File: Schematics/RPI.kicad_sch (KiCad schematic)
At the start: 1 part, among them J1 RPi GPIO

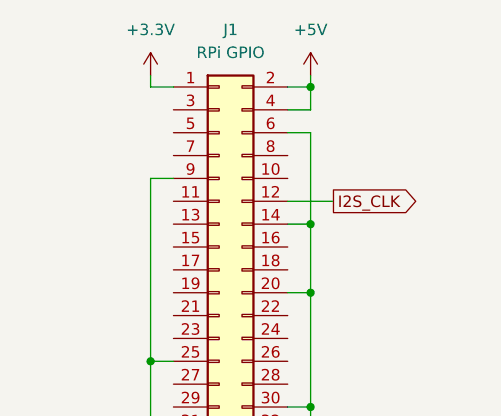
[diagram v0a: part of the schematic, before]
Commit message: Added recommended op-amps
Added recommended op-amps (without values) with dual mono TS in and out
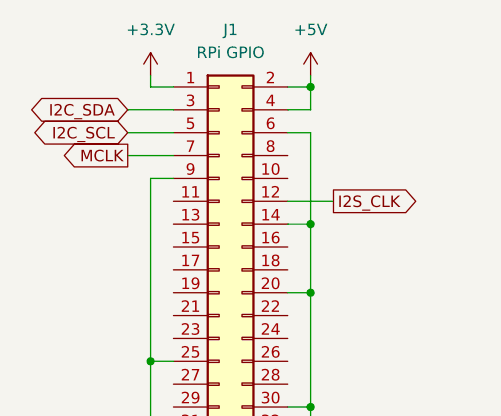
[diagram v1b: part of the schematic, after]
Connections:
- net I2C_SDA: now reaches J1.3 (Pin_3)
- net I2C_SCL: now reaches J1.5 (Pin_5)
- net MCLK: now reaches J1.7 (Pin_7)

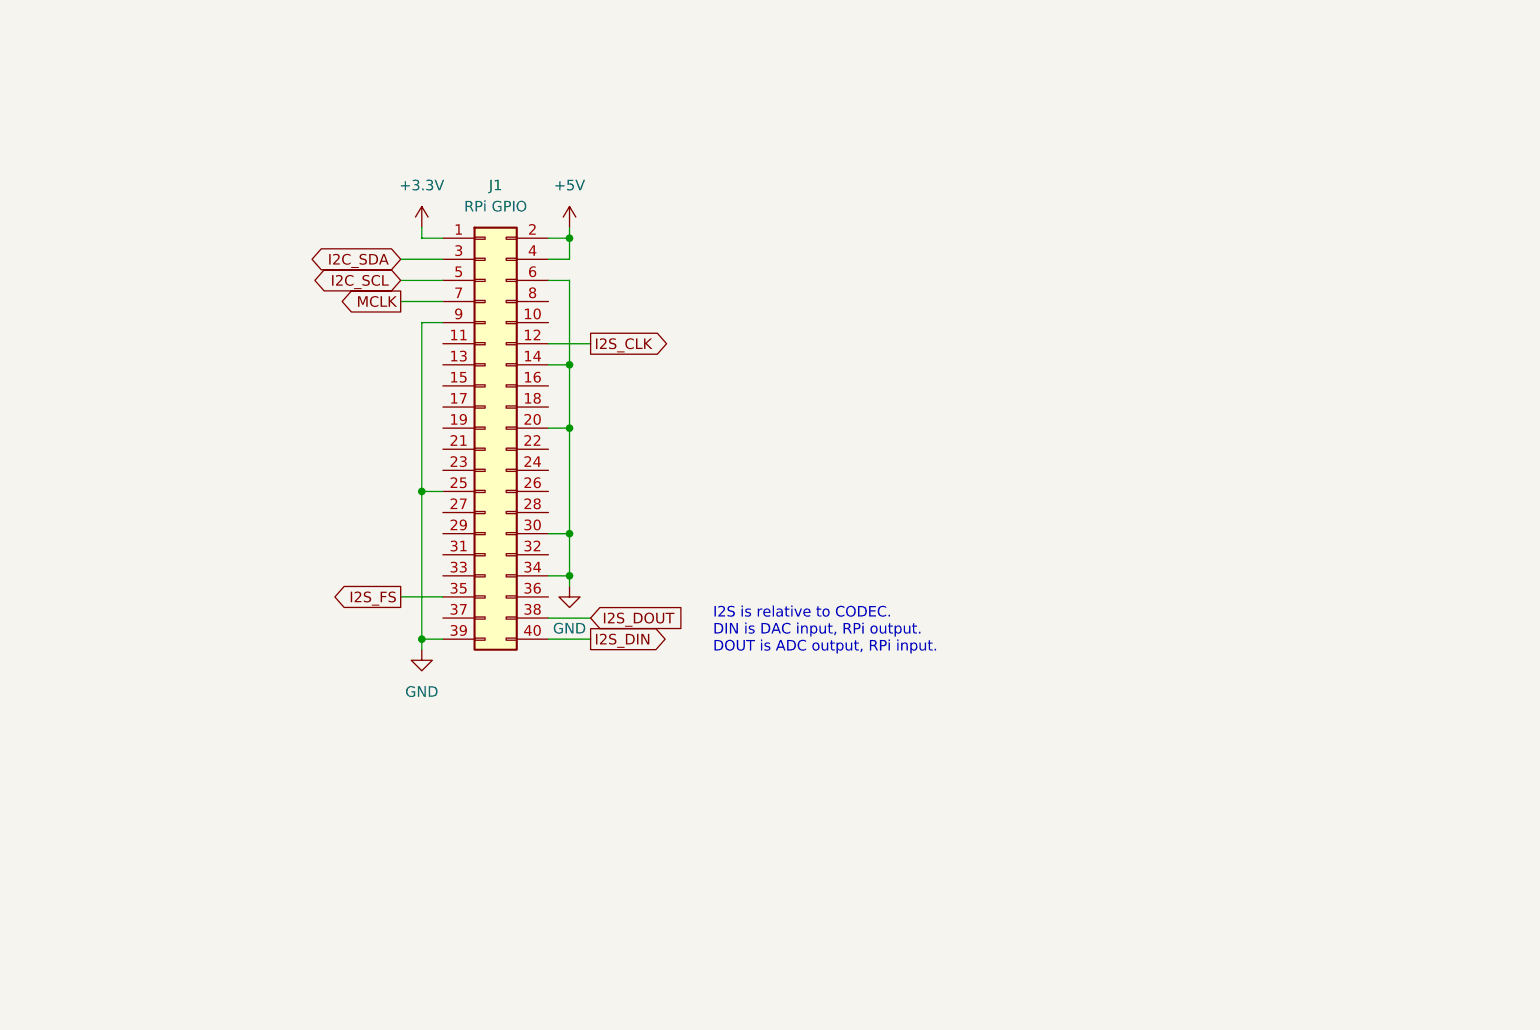
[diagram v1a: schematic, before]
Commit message: Input Buffer & EEPROM
line and instrument level buffers for the input added. EEPROM added and credits attributed !
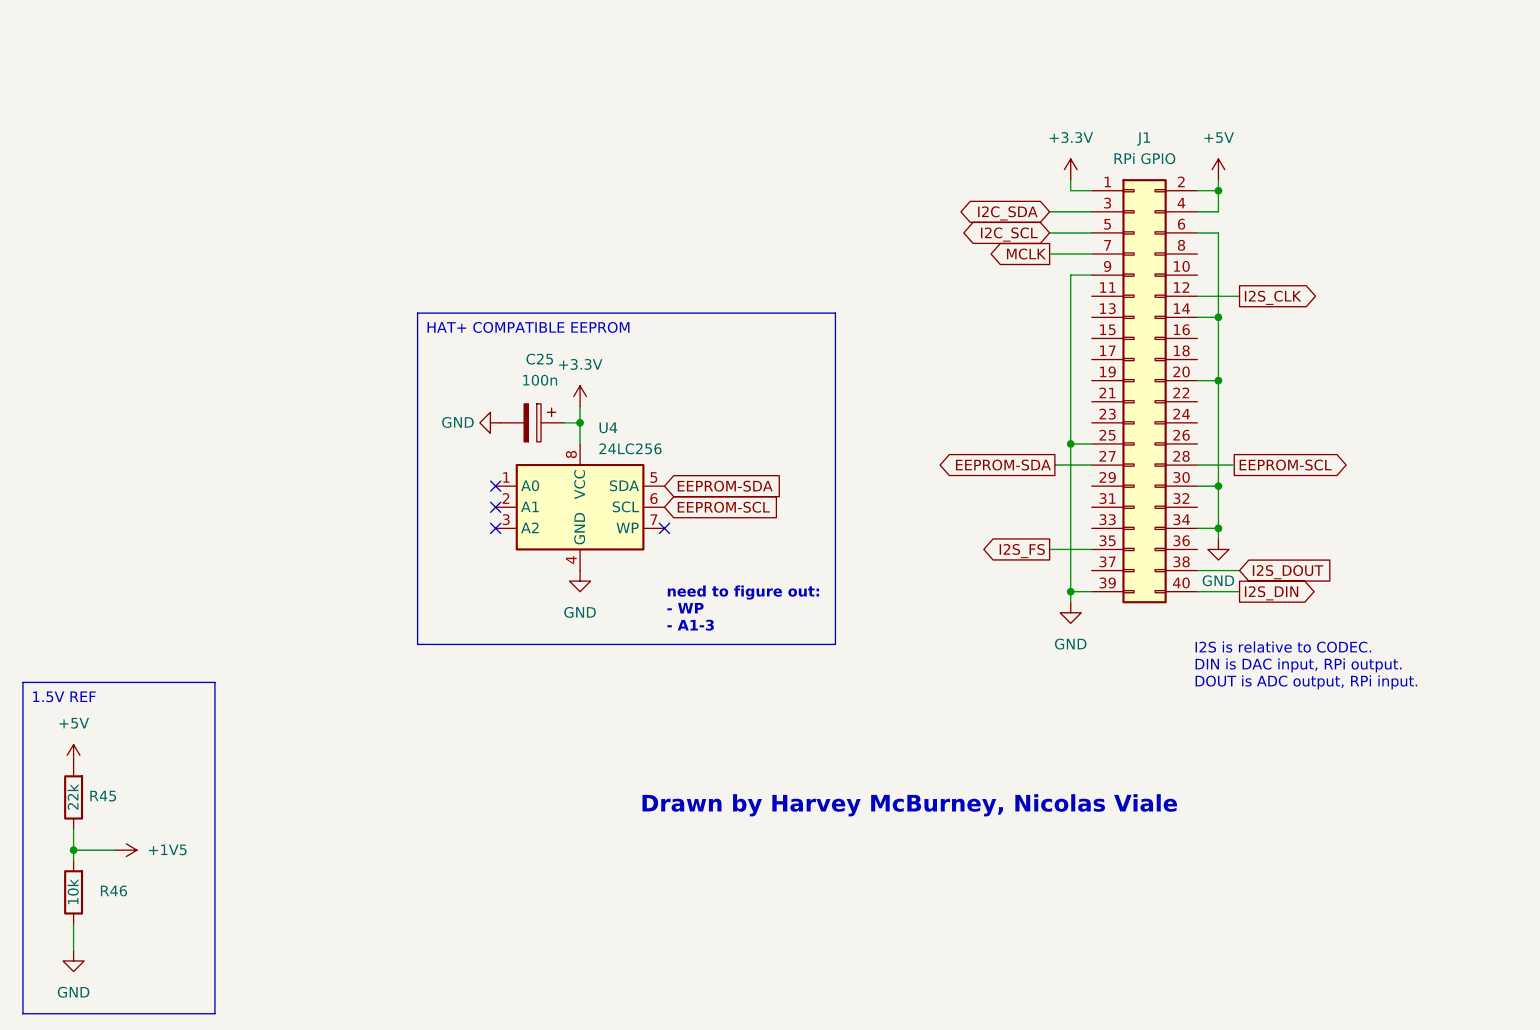
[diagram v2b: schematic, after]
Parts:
- added C25: 100n, symbol Device:C_Polarized
- added R45: 22k, symbol Device:R
- added R46: 10k, symbol Device:R
- added U4: 24LC256, symbol Memory_EEPROM:24LC256
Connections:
- net +3.3V: now also C25.1, U4.8 (VCC)
- net +5V: now also R45.2
- net GND: now also C25.2, R46.1, U4.4 (GND)
- net EEPROM-SDA: now reaches J1.27 (Pin_27)
- net EEPROM-SDA: now also U4.5 (SDA)
- net EEPROM-SCL: now reaches J1.28 (Pin_28)
- net EEPROM-SCL: now also U4.6 (SCL)
- new net +1V5: R45.1, R46.2
- no-connect marks 0 -> 4
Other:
- note added: "Drawn by Harvey McBurney, Nicolas Viale"
- note added: "need to figure out: - WP - A1-3"
- title: (none) -> Raspberry Pi GPIO pinout
- moved on the sheet: J1

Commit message: Schematic Update
Added EEPROM connections
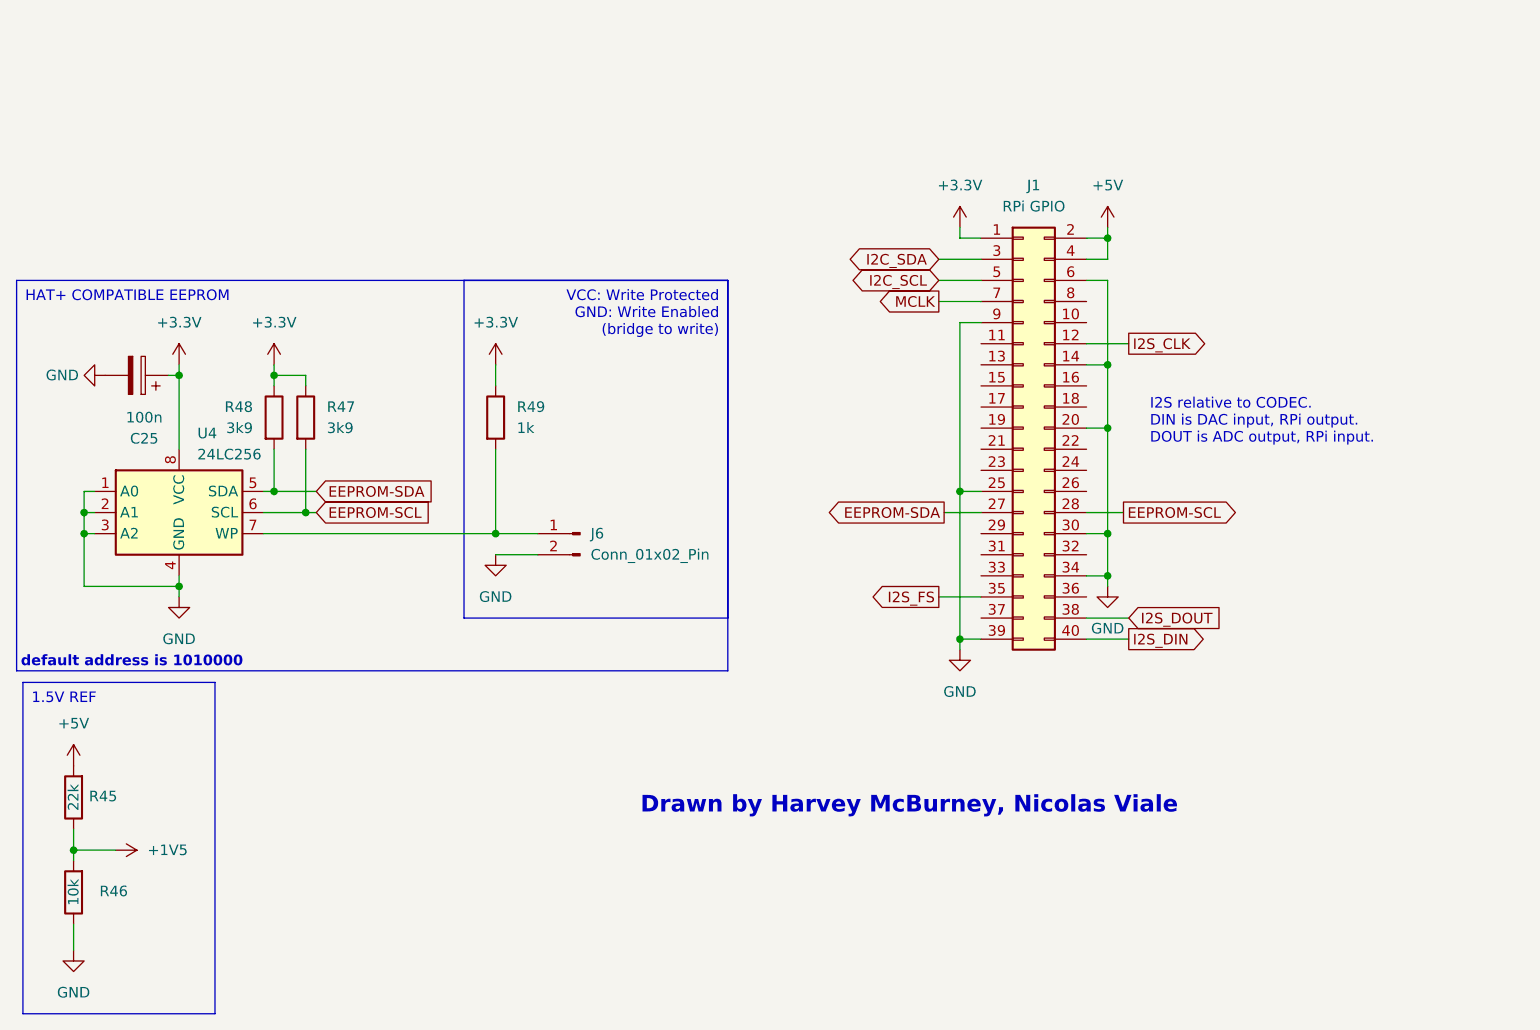
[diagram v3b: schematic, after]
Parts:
- added J6: Conn_01x02_Pin, symbol Connector:Conn_01x02_Pin
- added R47, R48: 3k9, symbol Device:R
- added R49: 1k, symbol Device:R
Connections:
- net +3.3V: now also R47.1, R48.1, R49.1
- net EEPROM-SCL: now also R47.2
- net EEPROM-SDA: now also R48.2
- net GND: now also U4.1 (A0), U4.2 (A1), U4.3 (A2), J6.2 (Pin_2)
- net at U4.7 (WP): now also J6.1 (Pin_1), R49.2
- no-connect marks 4 -> 0
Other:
- note added: "I2S relative to CODEC. DIN is DAC input, RPi output. DOUT is ADC output, RPi input."
- note added: "default address is 1010000"
- note removed: "I2S is relative to CODEC. DIN is DAC input, RPi output. DOUT is ADC output, RPi input."
- note removed: "need to figure out: - WP - A1-3"
- moved on the sheet: C25, J1, U4

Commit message: Added I/O Expander
I/O Expander added, 4 spare pins, still need to decouple.
Fixed some references to 3.3V, now all 3V3.
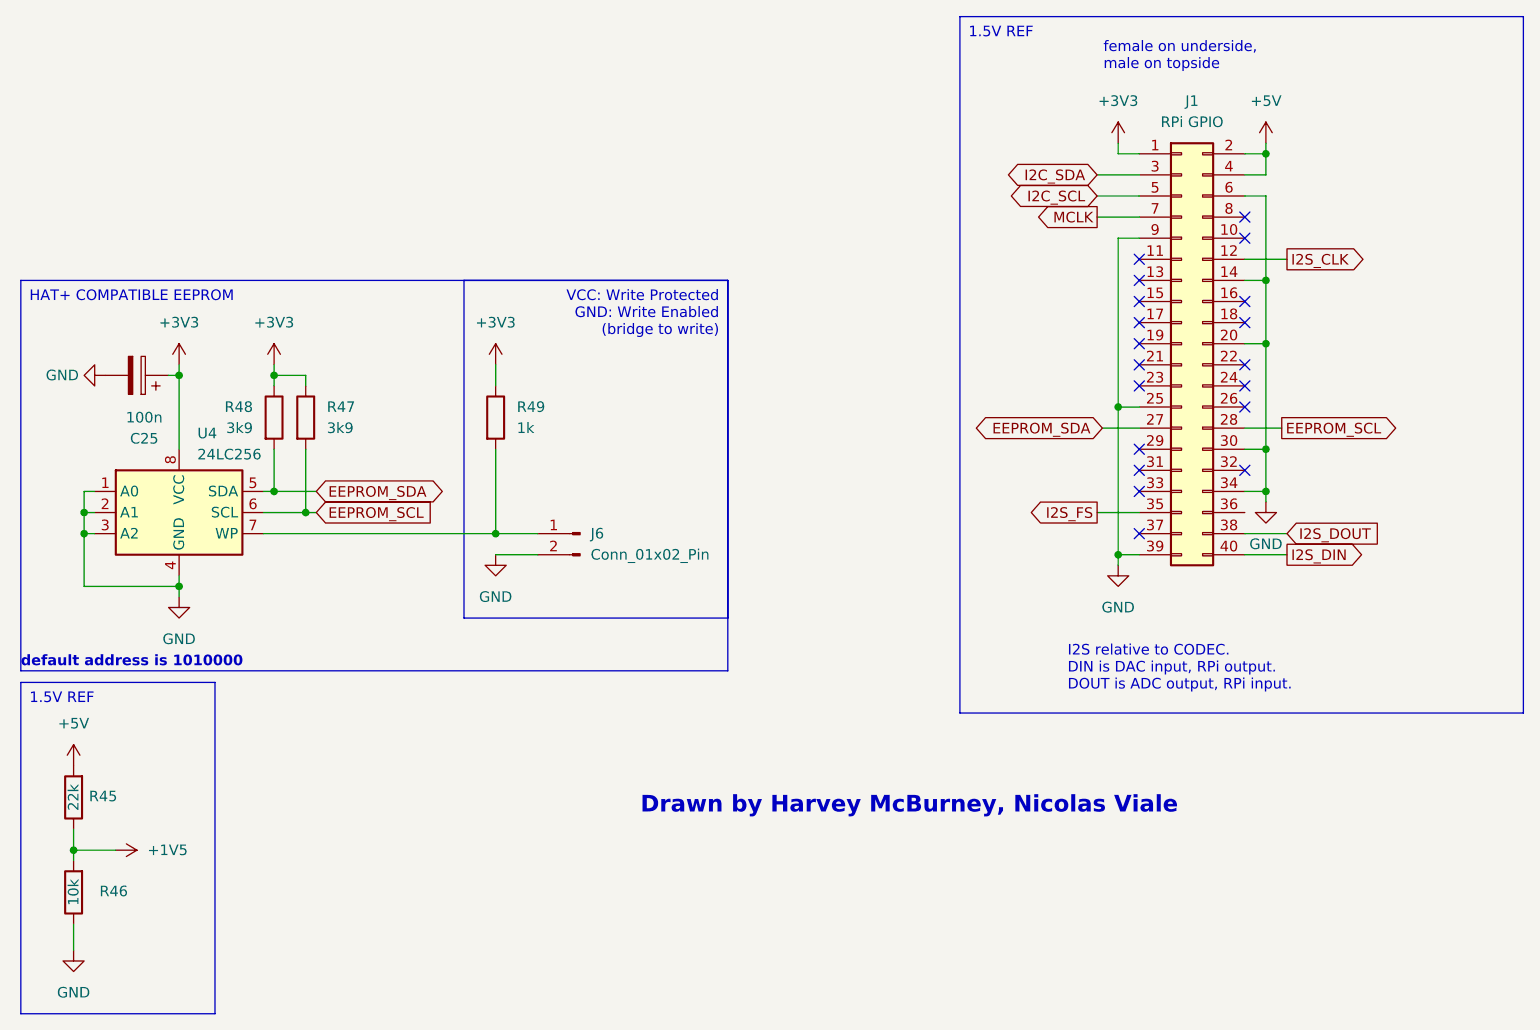
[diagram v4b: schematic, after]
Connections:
- net +3.3V renamed +3V3
- net EEPROM-SCL renamed EEPROM_SCL
- net EEPROM-SDA renamed EEPROM_SDA
- no-connect marks 0 -> 19
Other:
- note added: "female on underside, male on topside"
- moved on the sheet: J1

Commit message: Added Debug Headers
Added debug headers for I2C, I2S, and power. Also added m2.5 mounting holes for hat
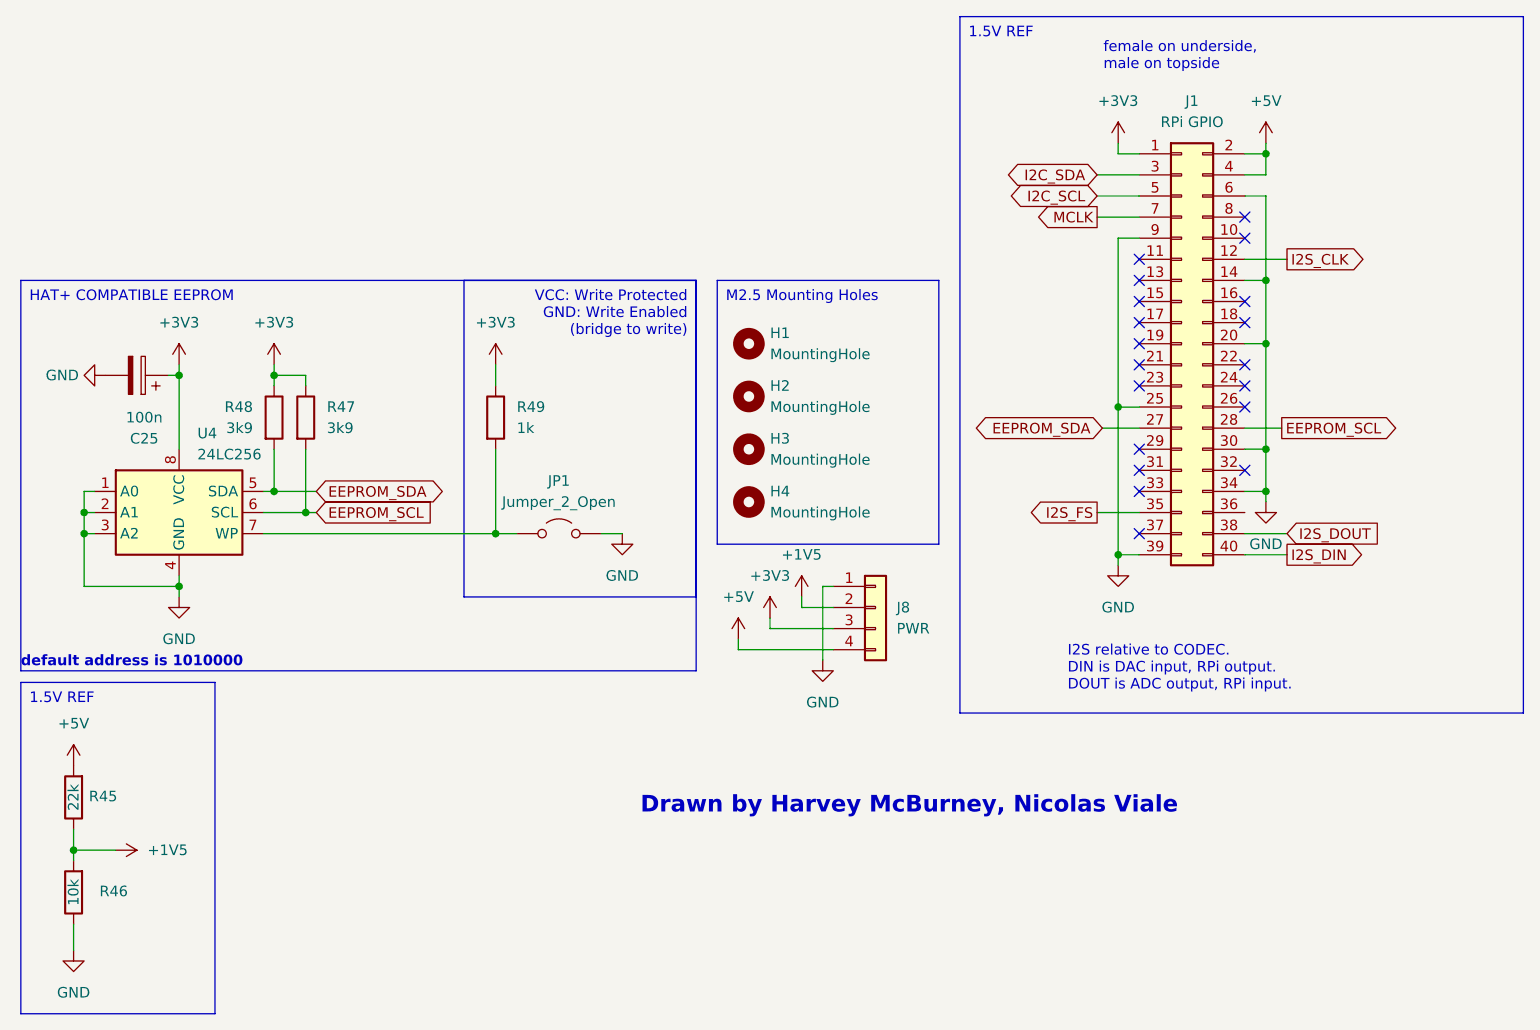
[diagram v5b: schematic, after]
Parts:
- removed J6: Conn_01x02_Pin, symbol Connector:Conn_01x02_Pin
- added H1, H2, H3, H4: MountingHole, symbol Mechanical:MountingHole
- added J8: PWR, symbol Connector_Generic:Conn_01x04
- added JP1: Jumper_2_Open, symbol Jumper:Jumper_2_Open
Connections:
- net +1V5: now also J8.2 (Pin_2)
- net +3V3: now also J8.3 (Pin_3)
- net +5V: now also J8.4 (Pin_4)
- net GND: now also J8.1 (Pin_1), JP1.2 (B)
- net at R49.2, U4.7 (WP): now also JP1.1 (A)
